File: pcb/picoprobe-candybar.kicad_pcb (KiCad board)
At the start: 2 copper layers, 0 parts

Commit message: First scratch compact board layout (ratsnest)
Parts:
- added A1: RaspberryPi_Pico, Module_RaspberryPi_Pico:RaspberryPi_Pico_Original_SMD_HandSolder, F.Cu at (101.6, 85.7)
- added C1: 1u, Capacitor_SMD:C_0805_2012Metric_Pad1.18x1.45mm_HandSolder, F.Cu at (104.8, 141.6)
- added C2: 1u, Capacitor_SMD:C_0805_2012Metric_Pad1.18x1.45mm_HandSolder, F.Cu at (90.2, 121.9)
- added C3: 1u, Capacitor_SMD:C_0805_2012Metric_Pad1.18x1.45mm_HandSolder, F.Cu at (90.2, 128.3)
- added C4: 1u, Capacitor_SMD:C_0805_2012Metric_Pad1.18x1.45mm_HandSolder, F.Cu at (90.2, 130.8)
- added C5: 1u, Capacitor_SMD:C_0805_2012Metric_Pad1.18x1.45mm_HandSolder, F.Cu at (90.2, 137.2)
- added C6: 1u, Capacitor_SMD:C_0805_2012Metric_Pad1.18x1.45mm_HandSolder, F.Cu at (101.6, 136.5)
- added C7: 1u, Capacitor_SMD:C_0805_2012Metric_Pad1.18x1.45mm_HandSolder, F.Cu at (101.6, 121.9)
- added D1: PMEG2010ER, Diode_SMD:Nexperia_CFP3_SOD-123W, F.Cu at (101.6, 156.2)
- added D2: Orange, LED_SMD:LED_0805_2012Metric_Pad1.15x1.40mm_HandSolder, F.Cu at (93.4, 157.5)
- added D3: Yellow, LED_SMD:LED_0805_2012Metric_Pad1.15x1.40mm_HandSolder, F.Cu at (93.4, 162.6)
- added D4: Green, LED_SMD:LED_0805_2012Metric_Pad1.15x1.40mm_HandSolder, F.Cu at (109.9, 157.5)
- added D5: Orange, LED_SMD:LED_0805_2012Metric_Pad1.15x1.40mm_HandSolder, F.Cu at (109.9, 162.6)
- added J0: SWD-UART_PicoprobeCandybar, Connector_PicoprobeCandybar:SWD-UART_PicoprobeCandybar_2Rows_7Pins_P2.54mm_Polarized_PressFit_Vertical, F.Cu at (103.1, 114.9)
- added J1: PinHeader_2x04, Connector_PinHeader_2.54mm:PinHeader_2x04_P2.54mm_Vertical, B.Cu at (97.8, 160.0)
- added J2: PinSocket_1x03, Connector_PinSocket_2.54mm:PinSocket_1x03_P2.54mm_Horizontal, B.Cu at (95.9, 129.5)
- added J3: PinSocket_1x02, Connector_PinSocket_2.54mm:PinSocket_1x02_P2.54mm_Horizontal, B.Cu at (95.9, 137.2)
- added J4: PinSocket_1x03, Connector_PinSocket_2.54mm:PinSocket_1x03_P2.54mm_Horizontal, B.Cu at (107.3, 134.6)
- added J5: PinSocket_1x03, Connector_PinSocket_2.54mm:PinSocket_1x03_P2.54mm_Horizontal, B.Cu at (107.3, 124.5)
- added J6: PinSocket_1x03, Connector_PinSocket_2.54mm:PinSocket_1x03_P2.54mm_Horizontal, B.Cu at (107.3, 114.3)
- added J7: PinSocket_1x01, Connector_PinSocket_2.54mm:PinSocket_1x01_P2.54mm_Horizontal, B.Cu at (107.3, 109.2)
- added Q1: T2N7002AK, Package_TO_SOT_SMD:SOT-23-3, F.Cu at (99.1, 141.6)
- added Q2: DMP31D1U, Package_TO_SOT_SMD:SOT-23-3, F.Cu at (92.7, 141.6)
- added R1: 470R, Resistor_SMD:R_0805_2012Metric_Pad1.20x1.40mm_HandSolder, F.Cu at (102.2, 141.6)
- added R10: 100R, Resistor_SMD:R_0805_2012Metric_Pad1.20x1.40mm_HandSolder, F.Cu at (90.2, 116.8)
- added R11: 100R, Resistor_SMD:R_0805_2012Metric_Pad1.20x1.40mm_HandSolder, F.Cu at (113.0, 133.3)
- added R12: 100R, Resistor_SMD:R_0805_2012Metric_Pad1.20x1.40mm_HandSolder, F.Cu at (113.0, 128.3)
- added R13: 100R, Resistor_SMD:R_0805_2012Metric_Pad1.20x1.40mm_HandSolder, F.Cu at (113.0, 125.7)
- added R14: 100R, Resistor_SMD:R_0805_2012Metric_Pad1.20x1.40mm_HandSolder, F.Cu at (113.0, 123.2)
- added R15: 470R, Resistor_SMD:R_0805_2012Metric_Pad1.20x1.40mm_HandSolder, F.Cu at (93.4, 154.9)
- added R16: 470R, Resistor_SMD:R_0805_2012Metric_Pad1.20x1.40mm_HandSolder, F.Cu at (93.4, 160.0)
- added R17: 470R, Resistor_SMD:R_0805_2012Metric_Pad1.20x1.40mm_HandSolder, F.Cu at (109.9, 154.9)
- added R18: 470R, Resistor_SMD:R_0805_2012Metric_Pad1.20x1.40mm_HandSolder, F.Cu at (109.9, 160.0)
- added R2: 100k, Resistor_SMD:R_0805_2012Metric_Pad1.20x1.40mm_HandSolder, F.Cu at (95.9, 141.6)
- added R3: 100R, Resistor_SMD:R_0805_2012Metric_Pad1.20x1.40mm_HandSolder, F.Cu at (90.2, 119.4)
- added R4: 100R, Resistor_SMD:R_0805_2012Metric_Pad1.20x1.40mm_HandSolder, F.Cu at (113.0, 141.0)
- added R5: 100R, Resistor_SMD:R_0805_2012Metric_Pad1.20x1.40mm_HandSolder, F.Cu at (90.2, 114.3)
- added R6: 100R, Resistor_SMD:R_0805_2012Metric_Pad1.20x1.40mm_HandSolder, F.Cu at (113.0, 135.9)
- added R7: 100R, Resistor_SMD:R_0805_2012Metric_Pad1.20x1.40mm_HandSolder, F.Cu at (113.0, 138.4)
- added R8: 100R, Resistor_SMD:R_0805_2012Metric_Pad1.20x1.40mm_HandSolder, F.Cu at (113.0, 143.5)
- added R9: 100R, Resistor_SMD:R_0805_2012Metric_Pad1.20x1.40mm_HandSolder, F.Cu at (113.0, 130.8)
- added SW1: SW-R1-1A-E-1-0, ProjectFootprints_PicoprobeCandybar:SW_Rocker_SPST_QuickConnect_P10.8mm_SW-R1-1X-E-XX-0_Retrofit-SMD-Horizontal, B.Cu at (85.1, 76.8)
- added SW2: SLW-156646-5A-N-D, ProjectFootprints_PicoprobeCandybar:SW_Slide_SP3T_Vertical_P3.2mm_CUI_SLW-156646-5A-N-D, F.Cu at (96.8, 149.2)
- added SW3: SLW-1277545-2A-RA-S-D, ProjectFootprints_PicoprobeCandybar:SW_Slide_SP3T_Common_Horizontal_P2mm_CUI_SLW-1277545-2A-RA-S-D, B.Cu at (88.9, 157.0)
- added U1: TLV77318PDBVR, Package_TO_SOT_SMD:SOT-23-5, F.Cu at (90.2, 125.1)
- added U2: TLV77325PDBVR, Package_TO_SOT_SMD:SOT-23-5, F.Cu at (90.2, 134.0)
- added U3: SN74LV6T17, Package_SO:TSSOP-14_4.4x5mm_P0.65mm, F.Cu at (101.6, 132.1)
- added U4: SN74LV6T17, Package_SO:TSSOP-14_4.4x5mm_P0.65mm, F.Cu at (101.6, 126.4)
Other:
- board outline added: 27.9 x 104.8 mm

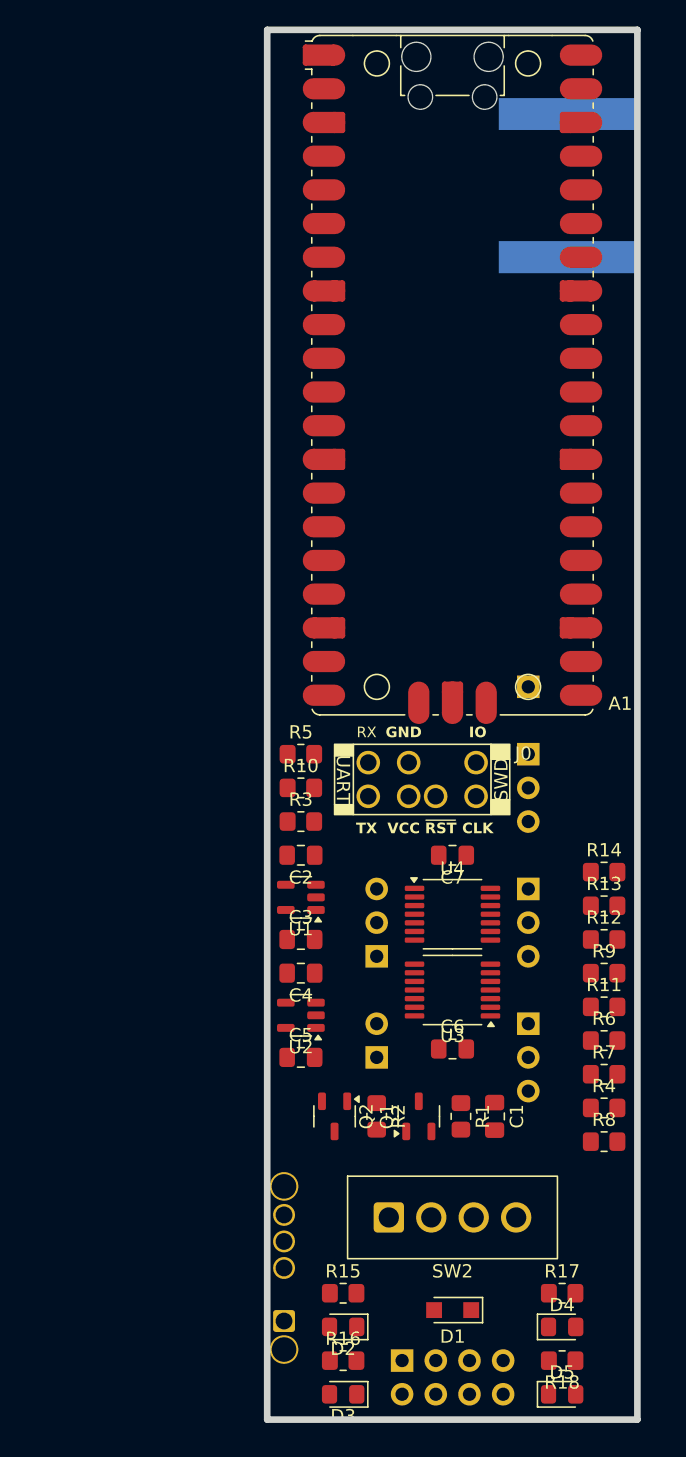
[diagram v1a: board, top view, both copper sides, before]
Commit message: Rework board layout
This is a large commit.  Aside from the new layout, it contains:
- Invert socket pin orders to simplify layout
- Expose ADC_VREF
- Resize board width
- Make board flush with Pico top (USB port)
- Use retrofit SMD for power switch (limited selection at 500mA 5V DC)
- More...

Intending to make sockets SMD, so ignore the intersecting through-holes.
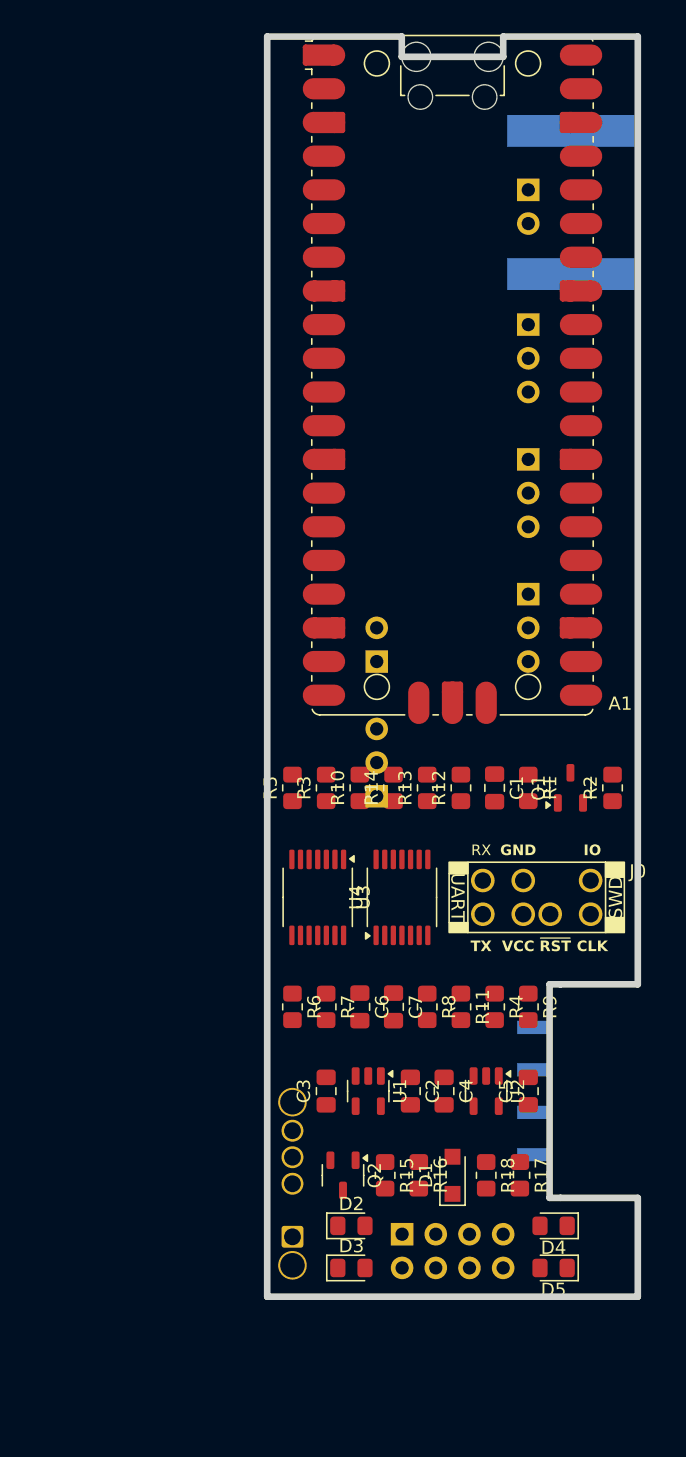
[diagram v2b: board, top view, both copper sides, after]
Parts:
- J7: value PinSocket_1x01 -> PinSocket_1x02; footprint Connector_PinSocket_2.54mm:PinSocket_1x01_P2.54mm_Horizontal -> Connector_PinSocket_2.54mm:PinSocket_1x02_P2.54mm_Horizontal
- SW2: footprint ProjectFootprints_PicoprobeCandybar:SW_Slide_SP3T_Vertical_P3.2mm_CUI_SLW-156646-5A-N-D -> ProjectFootprints_PicoprobeCandybar:SW_Slide_SP3T_P3.2mm_CUI_SLW-156646-5A-N-D_Retrofit-SMD-Horizontal; moved to B.Cu
- moved J7 37.5 mm to (107.3, 71.8)
- moved J4 32.4 mm to (107.3, 102.2)
- moved J5 32.4 mm to (107.3, 92.1)
- moved J6 32.4 mm to (107.3, 81.9)
- moved R2 30.5 mm to (113.7, 116.8), turned to 90 degrees
- moved J3 29.8 mm to (95.9, 107.3)
- moved Q1 27.3 mm to (110.5, 116.8)
- moved R1 25.3 mm to (107.3, 116.8)
- moved C1 24.8 mm to (104.8, 116.8)
- moved R6 23.6 mm to (89.5, 133.3), turned to -90 degrees
- moved R7 21.6 mm to (92.1, 133.3), turned to -90 degrees
- moved SW2 21.0 mm to (115.6, 139.7), turned to -90 degrees
- moved C2 19.6 mm to (98.4, 139.7), turned to -90 degrees
- moved C5 17.3 mm to (107.3, 139.7), turned to 90 degrees
- moved R14 17.1 mm to (97.2, 116.8), turned to 90 degrees
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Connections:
- A1 pad 35: unconnected-(A1-ADC_VREF-Pad35) -> /ADC_VREF
- J3 pad 1: /GPIO10 -> /GPIO11
- J3 pad 2: /GPIO11 -> /GPIO10
- J4 pad 1: /RSV_1 -> /RSV_3
- J4 pad 3: /RSV_3 -> /RSV_1
- J5 pad 1: /GPIO20 -> /GPIO22
- J5 pad 3: /GPIO22 -> /GPIO20
- J6 pad 1: /ADC0 -> /ADC2
- J6 pad 3: /ADC2 -> /ADC0
- J7 pad 1: AGND -> /ADC_VREF
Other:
- board size 27.9 x 104.8 mm -> 27.9 x 95 mm

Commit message: Start adding silkscreen labels
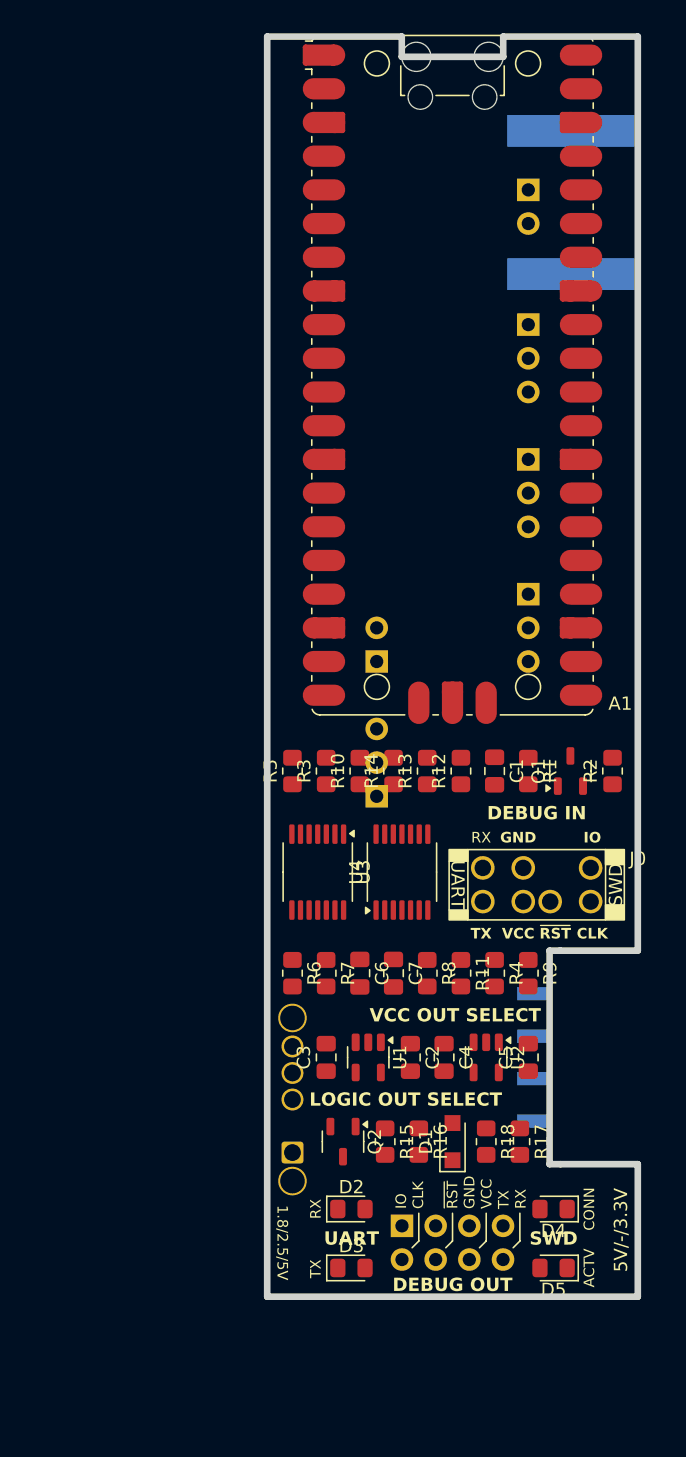
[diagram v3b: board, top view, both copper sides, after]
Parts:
- moved SW3 6.35 mm to (89.5, 144.3)
- moved D1 2.54 mm to (101.6, 143.5)
- moved Q2 2.54 mm to (93.3, 143.5)
- moved R15 2.54 mm to (96.5, 143.5)
- moved R16 2.54 mm to (99.1, 143.5)
- moved R17 2.54 mm to (106.7, 143.5)
- moved R18 2.54 mm to (104.1, 143.5)
- moved C2 2.54 mm to (98.4, 137.2)
- moved C3 2.54 mm to (92.1, 137.2)
- moved C4 2.54 mm to (101.0, 137.2)
- moved C5 2.54 mm to (107.3, 137.2)
- moved C6 2.54 mm to (94.6, 130.8)
- moved C7 2.54 mm to (97.2, 130.8)
- moved R11 2.54 mm to (102.2, 130.8)
- moved R4 2.54 mm to (104.8, 130.8)
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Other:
- outline, holes or cut-outs redrawn
- board text added: "1.8/2.5/5V"
- board text added: "5V/-/3.3V"
- board text added: "ACTV"
- board text added: "CONN"
- board text added: "DEBUG IN"
- board text added: "DEBUG OUT"
- board text added: "IO CLK ~{RST} GND VCC TX RX"
- board text added: "LOGIC OUT SELECT"
- board text added: "RX"
- board text added: "SWD"
- board text added: "TX"
- board text added: "UART"
- board text added: "VCC OUT SELECT"

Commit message: Add mounting holes
Also switches Pico footprint to have mounting holes
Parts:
- added REF**: MountingHole_2.2mm_M2_ISO7380, MountingHole:MountingHole_2.2mm_M2_ISO7380, F.Cu at (90.8, 150.5)
- added REF**: MountingHole_2.2mm_M2_ISO7380, MountingHole:MountingHole_2.2mm_M2_ISO7380, F.Cu at (112.4, 150.5)
- A1: footprint Module_RaspberryPi_Pico:RaspberryPi_Pico_Original_SMD_HandSolder -> Module_RaspberryPi_Pico:RaspberryPi_Pico_Original_SMD_MountingHoles_HandSolder
- moved D2 0.63 mm to (94.0, 148.0)
- moved D4 0.63 mm to (109.2, 148.0)
